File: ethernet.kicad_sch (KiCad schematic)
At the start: 51 parts, among them J1 L834-1G1T-S7, U20 KSZ9031RNXCA, Y2 ABM8G-25.000MHZ-18-D2Y-T3

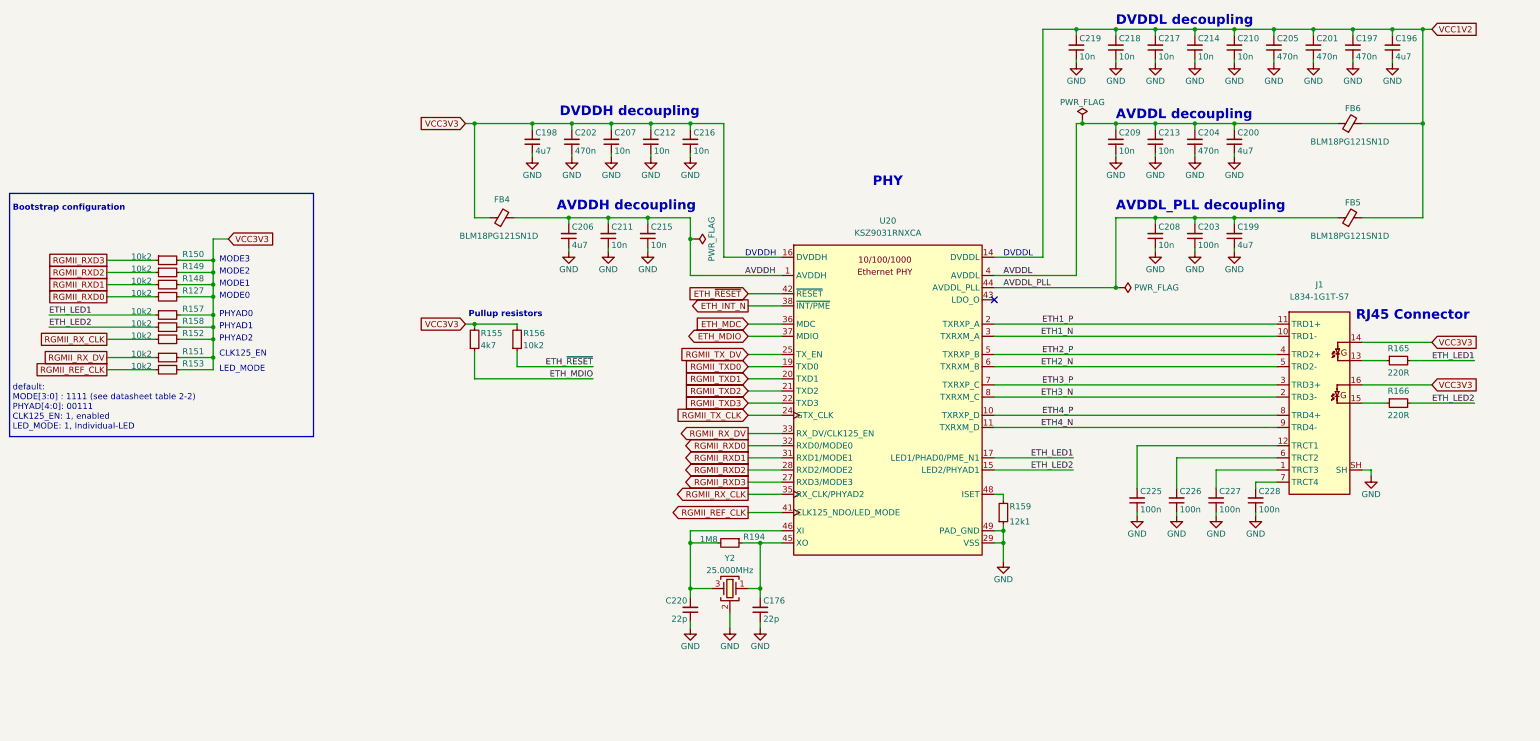
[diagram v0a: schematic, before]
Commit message: [#55652] Fix hotareas
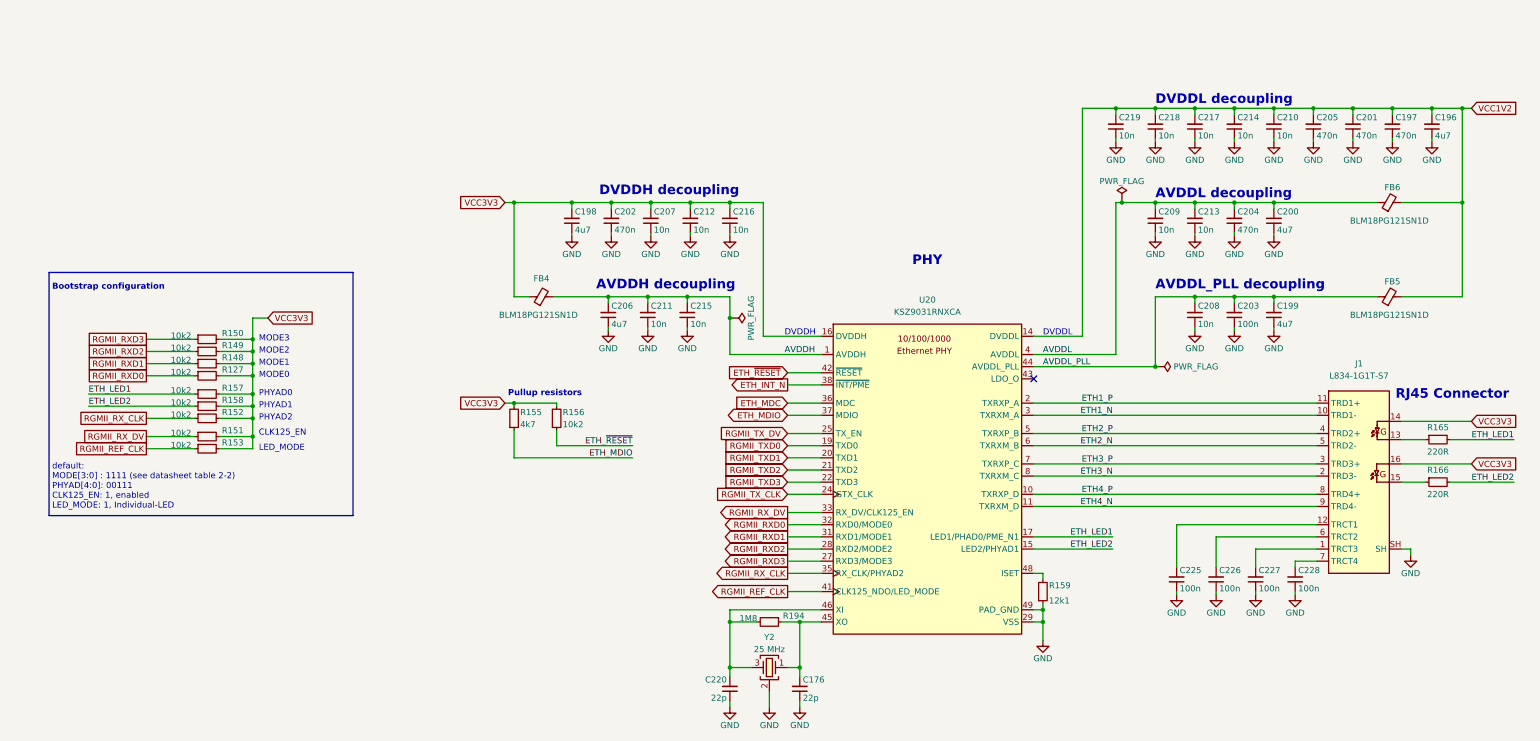
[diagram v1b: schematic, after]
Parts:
- C176, C220: Manufacturer Yaego -> YAGEO
- FB4, FB5, FB6: value FB_120Z_2A_0603 -> FB_120Z_2A_Murata-BLM18PG_0603; symbol antmicroFerriteBeadsandChips:FB_120Z_2A_0603 -> antmicroFerriteBeadsandChips:FB_120Z_2A_Murata-BLM18PG_0603
- J1: Manufacturer Bel Magnetic Solutions -> Bel Fuse
- U20: Manufacturer Microchip -> Microchip Technology
- Y2: value ABM8G-25.000MHZ-18-D2Y-T3 -> Resonator_25MHz_ABM8G; footprint antmicro-footprints:Oscillator_SMD_Geyer_KX-7-4Pin_3.2x2.5mm -> antmicro-footprints:Resonator_SMD_Abracon_ABM8G_3.2x2.5mm; symbol antmicroCrystals:ABM8G-25.000MHZ-18-D2Y-T3 -> antmicroResonators:Resonator_25MHz_ABM8G; Val 25.000MHz -> 25 MHz
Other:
- moved on the sheet: C176, C196, C197, C198, C199, C200, C201, C202, C203, C204, C205, C206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

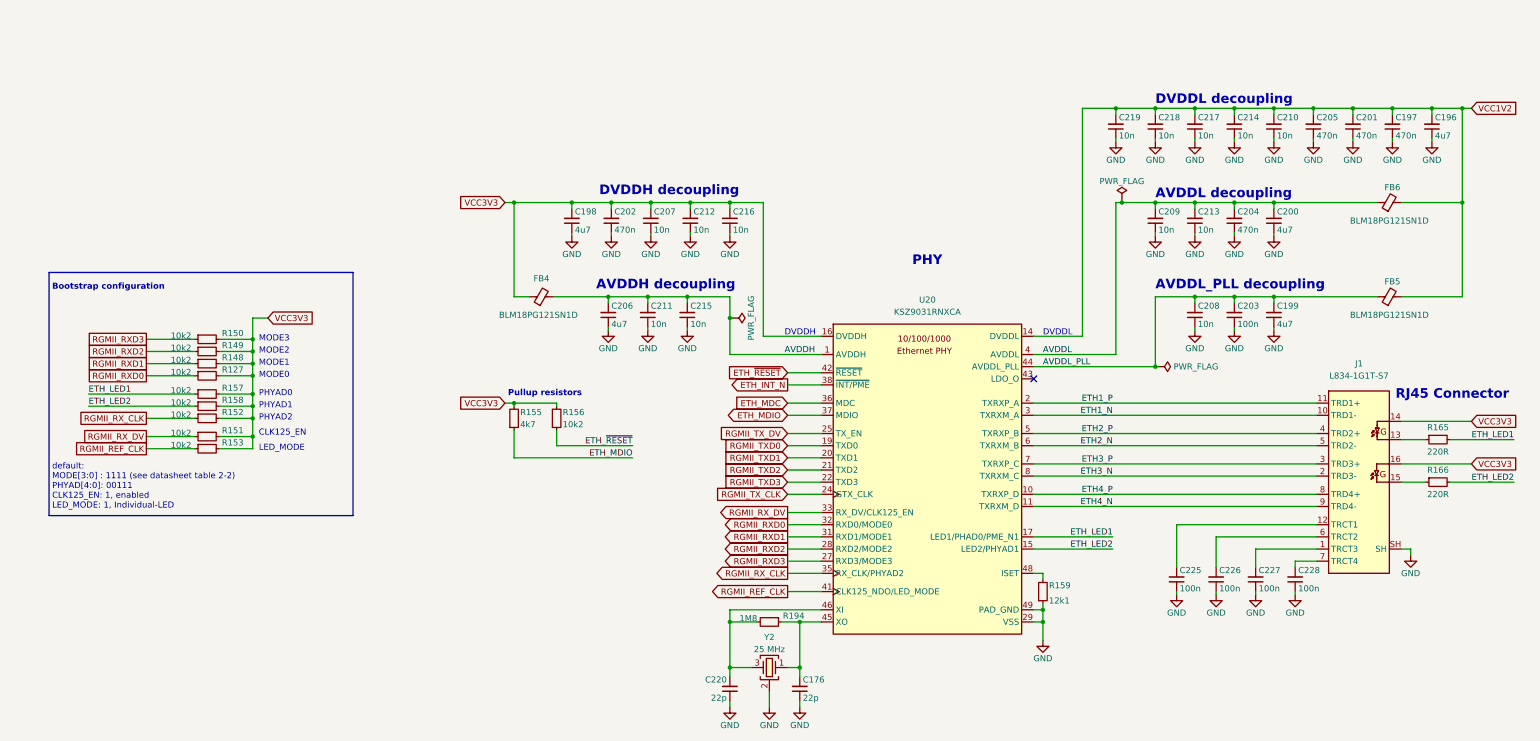
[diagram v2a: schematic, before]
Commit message: [#68236] Allign sch to grid
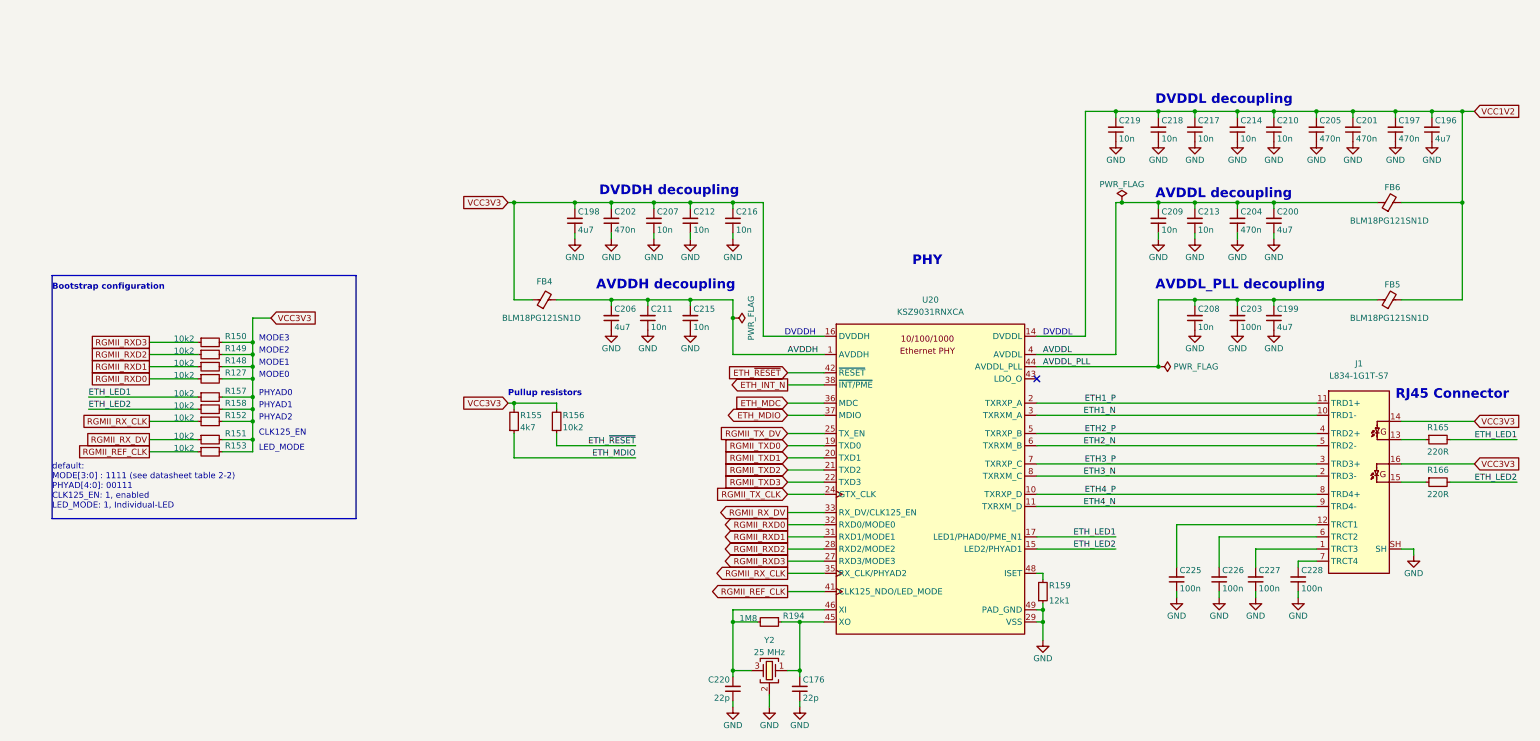
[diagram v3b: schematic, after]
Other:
- moved on the sheet: C196, C197, C198, C199, C201, C203, C204, C205, C206, C207, C208, C209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

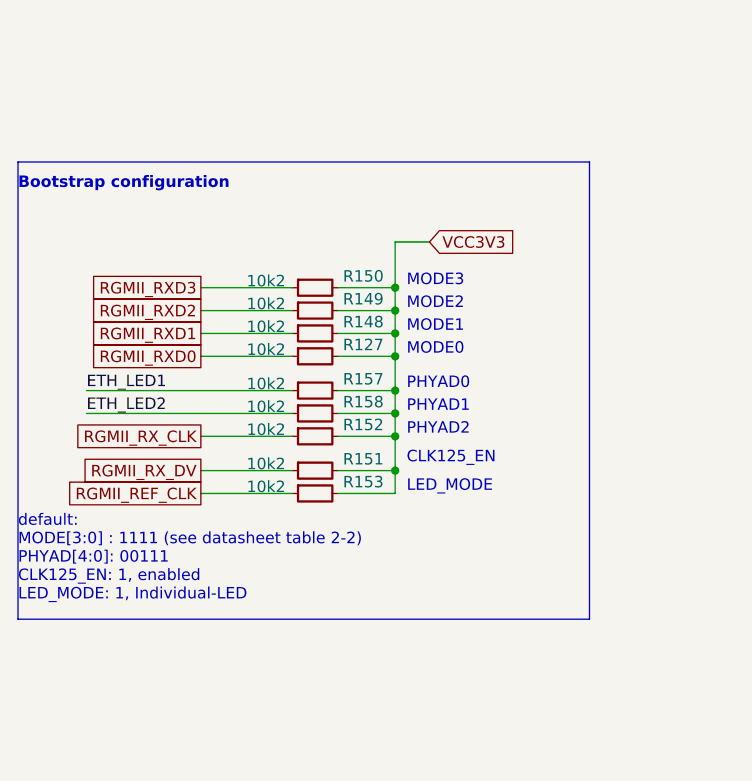
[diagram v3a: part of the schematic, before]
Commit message: [#68236] Remove DNP property from Testpoints
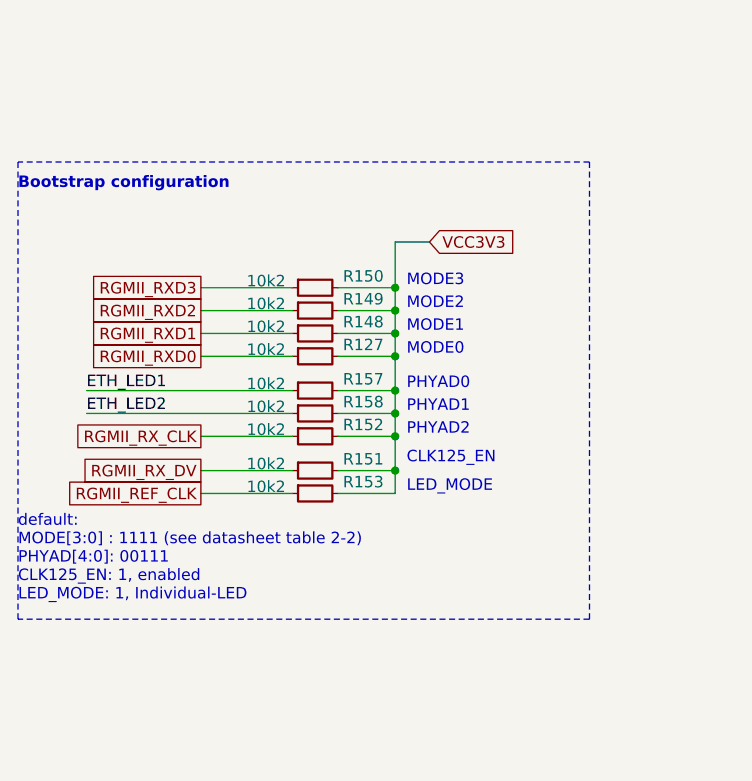
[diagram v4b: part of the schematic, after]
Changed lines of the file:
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@@
   )
   (polyline (pts (xy 99.06 101.6) (xy 99.06 152.4))
-    (stroke (width 0) (type solid))
+    (stroke (width 0) (type dash))
   )
   (wire (pts (xy 257.81 86.36) (xy 259.08 86.36))
@@
   )
   (polyline (pts (xy 35.56 152.4) (xy 35.56 101.6))
-    (stroke (width 0) (type solid))
+    (stroke (width 0) (type dash))
   )
   (wire (pts (xy 270.51 167.64) (xy 270.51 168.91))
@@
   )
   (polyline (pts (xy 99.06 101.6) (xy 35.56 101.6))
-    (stroke (width 0) (type solid))
+    (stroke (width 0) (type dash))
   )
   (wire (pts (xy 317.5 158.75) (xy 320.04 158.75))
@@
   )
   (polyline (pts (xy 99.06 152.4) (xy 35.56 152.4))
-    (stroke (width 0) (type solid))
+    (stroke (width 0) (type dash))
   )
   (wire (pts (xy 251.46 67.31) (xy 257.81 67.31))
